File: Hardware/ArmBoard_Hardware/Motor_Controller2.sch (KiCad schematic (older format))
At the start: 13 parts

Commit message: added missing lables to connectors
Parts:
- MC2: symbol MRDT_ICs:VNH5019A_E -> ArmBoard_Hardware-rescue:VNH5019A_E-MRDT_ICs
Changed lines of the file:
@@
 IN_A_2
 $Comp
-L MRDT_ICs:VNH5019A_E U?
+L ArmBoard_Hardware-rescue:VNH5019A_E-MRDT_ICs U?
 U 1 1 62E6C655
 P 4925 4600

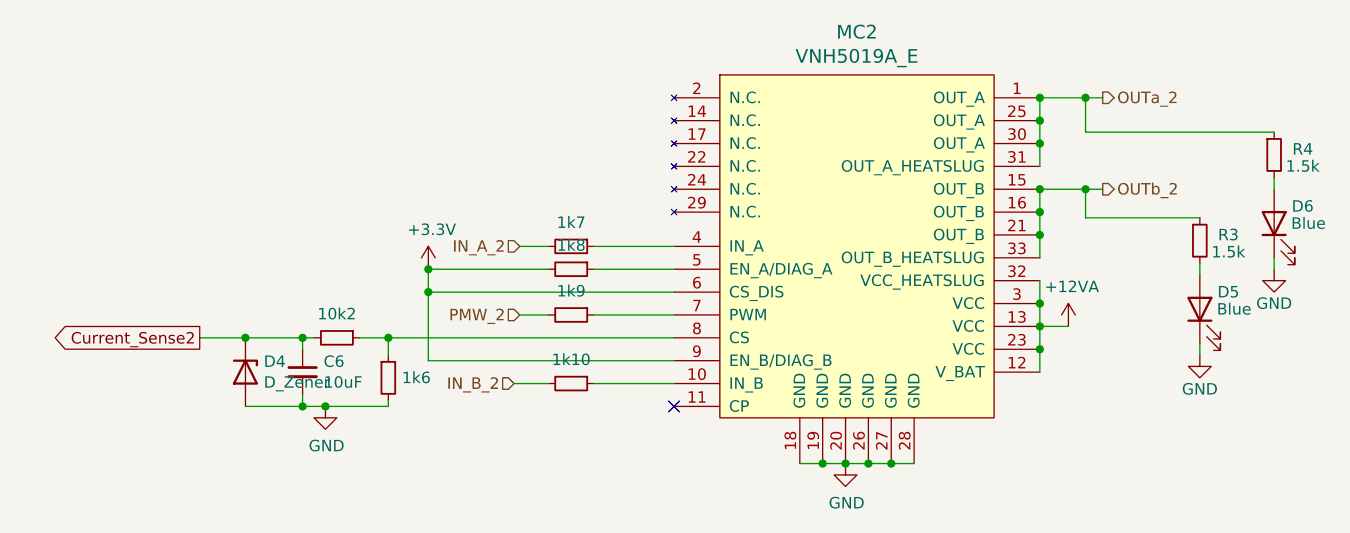
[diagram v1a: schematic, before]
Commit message: schematic changes, encoder changes, led changes
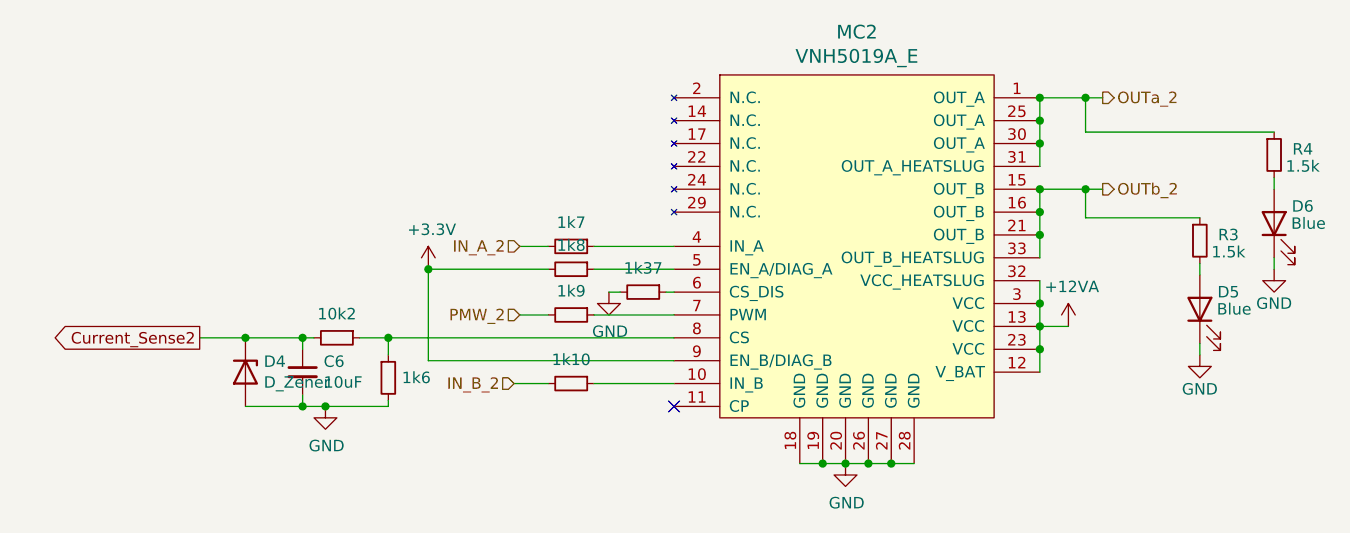
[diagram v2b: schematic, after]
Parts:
- added 1k37: R_Small, Resistor_SMD:R_0603_1608Metric_Pad0.98x0.95mm_HandSolder, symbol Device:R_Small
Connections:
- net +3V3: no longer MC2.6 (CS_DIS)
- net GND: now also 1k37.2
- new net: 1k37.1, MC2.6 (CS_DIS)
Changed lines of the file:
@@
 Wire Wire Line
 	4175 4150 4050 4150
-Wire Wire Line
-	4725 4050 3650 4050
-Wire Wire Line
-	3650 4050 3650 3950
 Connection ~ 3650 3950
 Wire Wire Line
 	4725 4350 3650 4350
-Wire Wire Line
-	3650 4350 3650 4050
-Connection ~ 3650 4050
 Wire Wire Line
 	4725 4250 3475 4250
@@
 Text HLabel 6600 3600 2    50   Output ~ 0
 OUTb_2
+Wire Wire Line
+	3650 3950 3650 4350
+$Comp
+L power:GND #PWR?
+U 1 1 62922784
+P 4440 4050
+AR Path="/63845F20/62922784" Ref="#PWR?"  Part="1"
+AR Path="/628CE14B/62922784" Ref="#PWR02"  Part="1"
+AR Path="/6297969A/62922784" Ref="#PWR?"  Part="1"
+AR Path="/629F46F6/62922784" Ref="#PWR?"  Part="1"
+AR Path="/629F46FD/62922784" Ref="#PWR?"  Part="1"
+AR Path="/62A5CC3B/62922784" Ref="#PWR?"  Part="1"
+AR Path="/62A5CC46/62922784" Ref="#PWR?"  Part="1"
+AR Path="/62AF9C52/62922784" Ref="#PWR?"  Part="1"
+AR Path="/62D2CE1B/62922784" Ref="#PWR?"  Part="1"
+F 0 "#PWR02" H 4440 3800 50  0001 C CNN
+F 1 "GND" H 4445 3877 50  0000 C CNN
+F 2 "" H 4440 4050 50  0001 C CNN
+F 3 "" H 4440 4050 50  0001 C CNN
+	1    4440 4050
+	1    0    0    -1
+$EndComp
+$Comp
+L Device:R_Small 1k?
+U 1 1 6292278A
+P 4590 4050
+AR Path="/63845F20/6292278A" Ref="1k?"  Part="1"
+AR Path="/628CE14B/6292278A" Ref="1k37"  Part="1"
+AR Path="/6297969A/6292278A" Ref="1k?"  Part="1"
+AR Path="/629F46F6/6292278A" Ref="1k?"  Part="1"
+AR Path="/629F46FD/6292278A" Ref="1k?"  Part="1"
+AR Path="/62A5CC3B/6292278A" Ref="1k?"  Part="1"
+AR Path="/62A5CC46/6292278A" Ref="1k?"  Part="1"
+AR Path="/62AF9C52/6292278A" Ref="1k?"  Part="1"
+AR Path="/62C19165/6292278A" Ref="1k?"  Part="1"
+AR Path="/62CA8FD7/6292278A" Ref="1k?"  Part="1"
+AR Path="/62CBA1AC/6292278A" Ref="1k?"  Part="1"
+AR Path="/62CCE879/6292278A" Ref="1k?"  Part="1"
+AR Path="/62CE0B38/6292278A" Ref="1k?"  Part="1"
+AR Path="/62CF1227/6292278A" Ref="1k?"  Part="1"
+AR Path="/62D0C672/6292278A" Ref="1k?"  Part="1"
+AR Path="/62D1BEB1/6292278A" Ref="1k?"  Part="1"
+AR Path="/62D2CE1B/6292278A" Ref="1k?"  Part="1"
+AR Path="/62D3BCB9/6292278A" Ref="1k?"  Part="1"
+AR Path="/62D4BAA1/6292278A" Ref="1k?"  Part="1"
+F 0 "1k37" V 4486 4050 50  0000 C CNN
+F 1 "R_Small" V 4485 4050 50  0001 C CNN
+F 2 "Resistor_SMD:R_0603_1608Metric_Pad0.98x0.95mm_HandSolder" H 4590 4050 50  0001 C CNN
+F 3 "~" H 4590 4050 50  0001 C CNN
+	1    4590 4050
+	0    1    1    0
+$EndComp
+Wire Wire Line
+	4440 4050 4490 4050
+Wire Wire Line
+	4690 4050 4725 4050
 $EndSCHEMATC

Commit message: gerbs added and zipped
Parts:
- MC2: symbol ArmBoard_Hardware-rescue:VNH5019A_E-MRDT_ICs -> MRDT_ICs:VNH5019A_E
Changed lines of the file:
@@
 IN_A_2
 $Comp
-L ArmBoard_Hardware-rescue:VNH5019A_E-MRDT_ICs U?
+L MRDT_ICs:VNH5019A_E U?
 U 1 1 62E6C655
 P 4925 4600
